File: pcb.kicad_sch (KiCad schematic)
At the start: 13 parts

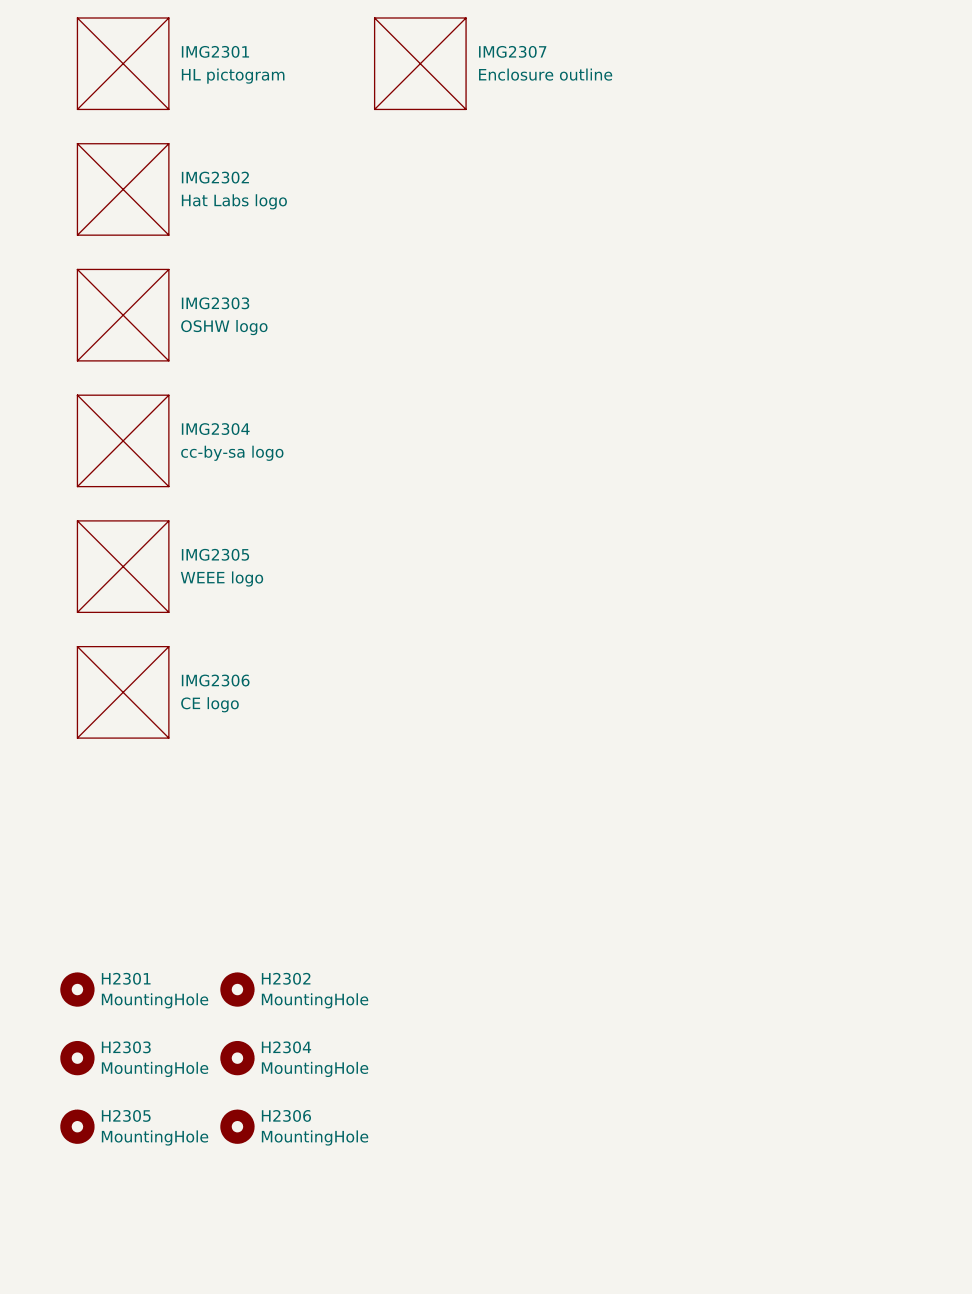
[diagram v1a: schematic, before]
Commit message: Reannotate components
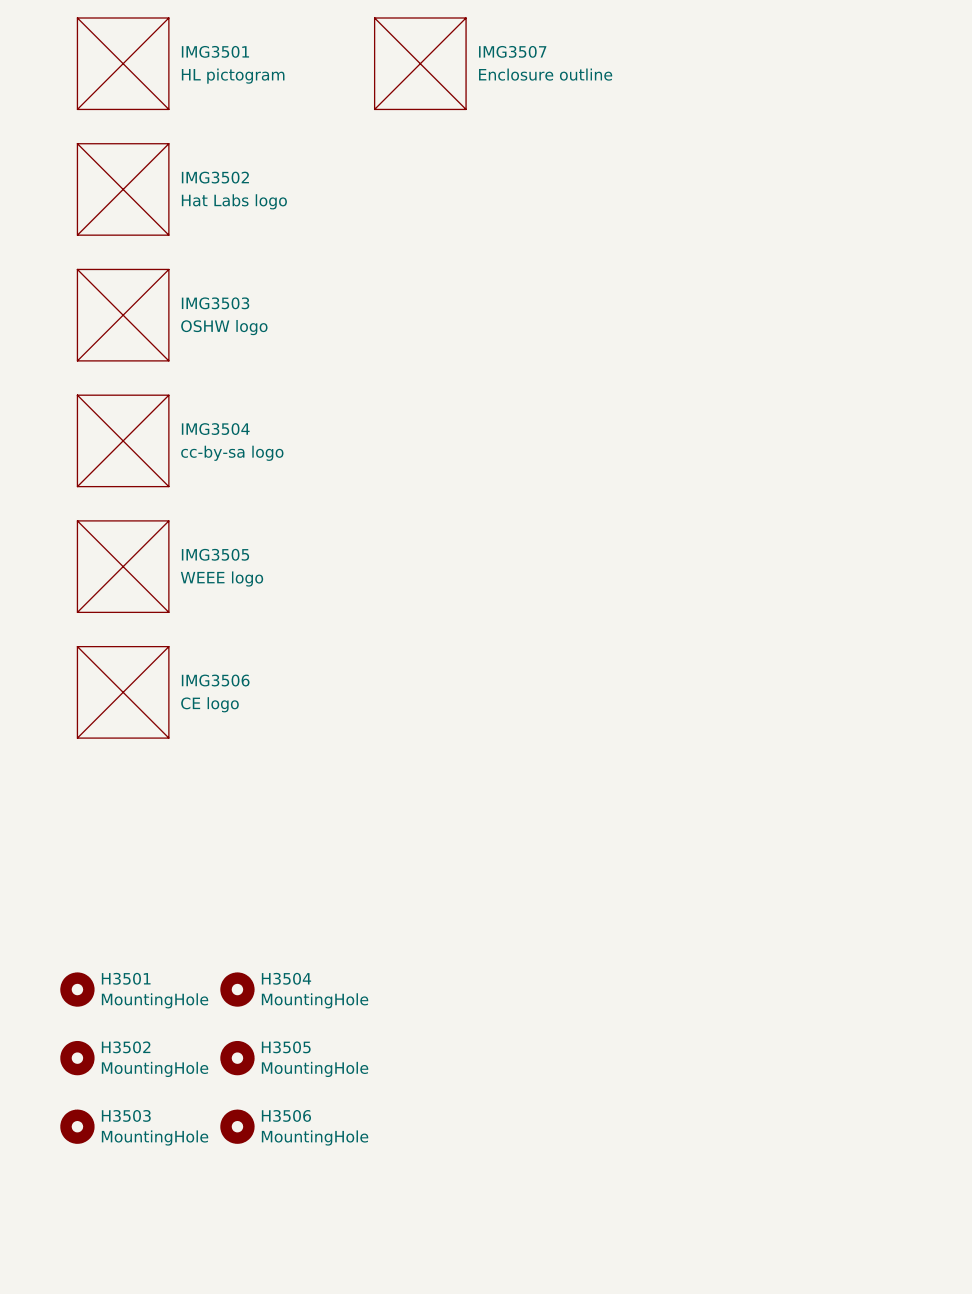
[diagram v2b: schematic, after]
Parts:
- renumbered H2301 to H3501, H2303 to H3502, H2305 to H3503, H2302 to H3504, H2304 to H3505, H2306 to H3506, IMG2301 to IMG3501, IMG2302 to IMG3502, IMG2303 to IMG3503, IMG2304 to IMG3504, IMG2305 to IMG3505, IMG2306 to IMG3506, IMG2307 to IMG3507
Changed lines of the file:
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@@
 		(dnp no)
 		(fields_autoplaced yes)
-		(property "Reference" "IMG2305"
+		(property "Reference" "IMG3505"
 			(at 52.07 92.7099 0)
 			(effects
@@
 			(project "HALPI2"
 				(path "/abc482bd-3f17-4d35-80db-1da3dcdb5c27/e4643111-53ad-48d1-8ad1-a500e184f609"
-					(reference "IMG2305")
+					(reference "IMG3505")
 					(unit 1)
 				)
@@
 		(on_board yes)
 		(dnp no)
-		(property "Reference" "H2306"
+		(property "Reference" "H3506"
 			(at 60.9601 155.0606 0)
 			(effects
@@
 			(project "HALPI2"
 				(path "/abc482bd-3f17-4d35-80db-1da3dcdb5c27/e4643111-53ad-48d1-8ad1-a500e184f609"
-					(reference "H2306")
+					(reference "H3506")
 					(unit 1)
 				)
@@
 		(dnp no)
 		(fields_autoplaced yes)
-		(property "Reference" "IMG2302"
+		(property "Reference" "IMG3502"
 			(at 52.07 50.7999 0)
 			(effects
@@
 			(project "HALPI2"
 				(path "/abc482bd-3f17-4d35-80db-1da3dcdb5c27/e4643111-53ad-48d1-8ad1-a500e184f609"
-					(reference "IMG2302")
+					(reference "IMG3502")
 					(unit 1)
 				)
@@
 		(dnp no)
 		(fields_autoplaced yes)
-		(property "Reference" "IMG2303"
+		(property "Reference" "IMG3503"
 			(at 52.07 64.7699 0)
 			(effects
@@
 			(project "HALPI2"
 				(path "/abc482bd-3f17-4d35-80db-1da3dcdb5c27/e4643111-53ad-48d1-8ad1-a500e184f609"
-					(reference "IMG2303")
+					(reference "IMG3503")
 					(unit 1)
 				)
@@
 		(on_board yes)
 		(dnp no)
-		(property "Reference" "H2302"
+		(property "Reference" "H3504"
 			(at 60.9601 139.8206 0)
 			(effects
@@
 			(project "HALPI2"
 				(path "/abc482bd-3f17-4d35-80db-1da3dcdb5c27/e4643111-53ad-48d1-8ad1-a500e184f609"
-					(reference "H2302")
+					(reference "H3504")
 					(unit 1)
 				)
@@
 		(on_board yes)
 		(dnp no)
-		(property "Reference" "H2304"
+		(property "Reference" "H3505"
 			(at 60.9601 147.4406 0)
 			(effects
@@
 			(project "HALPI2"
 				(path "/abc482bd-3f17-4d35-80db-1da3dcdb5c27/e4643111-53ad-48d1-8ad1-a500e184f609"
-					(reference "H2304")
+					(reference "H3505")
 					(unit 1)
 				)
@@
 		(on_board yes)
 		(dnp no)
-		(property "Reference" "H2303"
+		(property "Reference" "H3502"
 			(at 43.1801 147.4406 0)
 			(effects
@@
 			(project "HALPI2"
 				(path "/abc482bd-3f17-4d35-80db-1da3dcdb5c27/e4643111-53ad-48d1-8ad1-a500e184f609"
-					(reference "H2303")
+					(reference "H3502")
 					(unit 1)
 				)
@@
 		(dnp no)
 		(fields_autoplaced yes)
-		(property "Reference" "IMG2304"
+		(property "Reference" "IMG3504"
 			(at 52.07 78.7399 0)
 			(effects
@@
 			(project "HALPI2"
 				(path "/abc482bd-3f17-4d35-80db-1da3dcdb5c27/e4643111-53ad-48d1-8ad1-a500e184f609"
-					(reference "IMG2304")
+					(reference "IMG3504")
 					(unit 1)
 				)
@@
 		(dnp no)
 		(fields_autoplaced yes)
-		(property "Reference" "IMG2307"
+		(property "Reference" "IMG3507"
 			(at 85.09 36.8299 0)
 			(effects
@@
 			(project "HALPI2"
 				(path "/abc482bd-3f17-4d35-80db-1da3dcdb5c27/e4643111-53ad-48d1-8ad1-a500e184f609"
-					(reference "IMG2307")
+					(reference "IMG3507")
 					(unit 1)
 				)
@@
 		(on_board yes)
 		(dnp no)
-		(property "Reference" "H2301"
+		(property "Reference" "H3501"
 			(at 43.1801 139.8206 0)
 			(effects
@@
 			(project "HALPI2"
 				(path "/abc482bd-3f17-4d35-80db-1da3dcdb5c27/e4643111-53ad-48d1-8ad1-a500e184f609"
-					(reference "H2301")
+					(reference "H3501")
 					(unit 1)
 				)
@@
 		(dnp no)
 		(fields_autoplaced yes)
-		(property "Reference" "IMG2301"
+		(property "Reference" "IMG3501"
 			(at 52.07 36.8299 0)
 			(effects
@@
 			(project "HALPI2"
 				(path "/abc482bd-3f17-4d35-80db-1da3dcdb5c27/e4643111-53ad-48d1-8ad1-a500e184f609"
-					(reference "IMG2301")
+					(reference "IMG3501")
 					(unit 1)
 				)
@@
 		(on_board yes)
 		(dnp no)
-		(property "Reference" "H2305"
+		(property "Reference" "H3503"
 			(at 43.1801 155.0606 0)
 			(effects
@@
 			(project "HALPI2"
 				(path "/abc482bd-3f17-4d35-80db-1da3dcdb5c27/e4643111-53ad-48d1-8ad1-a500e184f609"
-					(reference "H2305")
+					(reference "H3503")
 					(unit 1)
 				)
@@
 		(dnp no)
 		(fields_autoplaced yes)
-		(property "Reference" "IMG2306"
+		(property "Reference" "IMG3506"
 			(at 52.07 106.6799 0)
 			(effects
@@
 			(project "HALPI2"
 				(path "/abc482bd-3f17-4d35-80db-1da3dcdb5c27/e4643111-53ad-48d1-8ad1-a500e184f609"
-					(reference "IMG2306")
-					(unit 1)
-				)
+					(reference "IMG3506")
+					(unit 1)
+				)

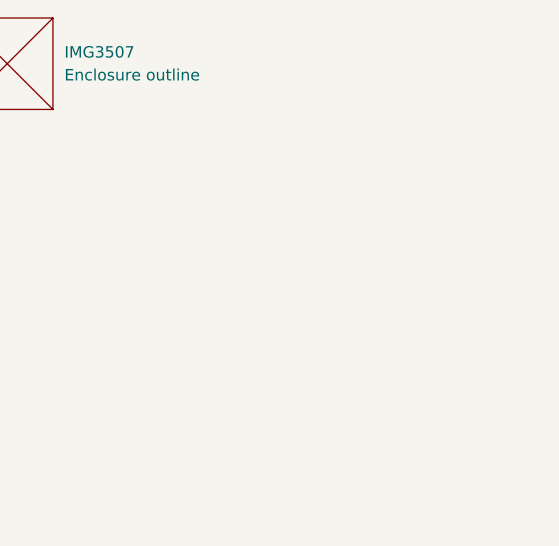
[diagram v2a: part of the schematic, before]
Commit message: Most DRC errors fixed
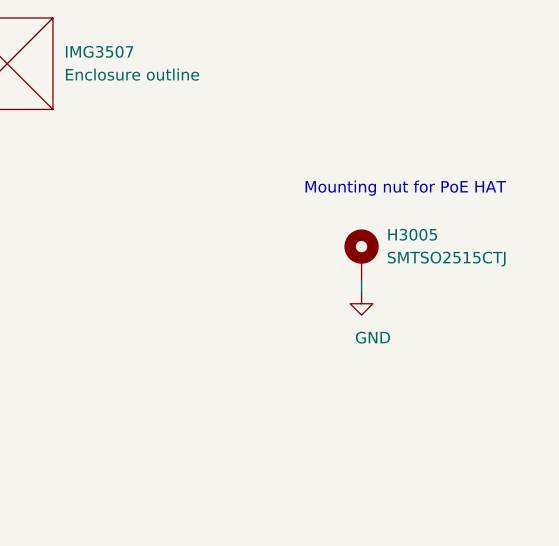
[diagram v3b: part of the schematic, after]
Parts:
- added H3005: SMTSO2515CTJ, Hatlabs:SMTSO2515CTJ, symbol Mechanical:MountingHole_Pad
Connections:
- new net GND: H3005.1
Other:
- note added: "Mounting nut for PoE HAT"
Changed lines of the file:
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@@
 		(comment 3 "HALPI2 is licensed under CERN-OHL-S v2.")
+	)
+	(text "Mounting nut for PoE HAT"
+		(exclude_from_sim no)
+		(at 122.936 52.07 0)
+		(effects
+			(font
+				(size 1.27 1.27)
+			)
+		)
+	)
+	(wire
+		(pts
+			(xy 118.11 63.5) (xy 118.11 62.23)
+		)
+		(stroke
+			(width 0)
+			(type default)
+		)
 	)
 	(symbol
@@
 	)
 	(symbol
+		(lib_id "power:GND")
+		(at 118.11 63.5 0)
+		(unit 1)
+		(exclude_from_sim no)
+		(in_bom yes)
+		(on_board yes)
+		(dnp no)
+		(property "Reference" "#PWR03009"
+			(at 118.11 69.85 0)
+			(effects
+				(font
+					(size 1.27 1.27)
+				)
+				(hide yes)
+			)
+		)
+		(property "Value" "GND"
+			(at 119.38 68.58 0)
+			(effects
+				(font
+					(size 1.27 1.27)
+				)
+			)
+		)
+		(property "Footprint" ""
+			(at 118.11 63.5 0)
+			(effects
+				(font
+					(size 1.27 1.27)
+				)
+				(hide yes)
+			)
+		)
+		(property "Datasheet" ""
+			(at 118.11 63.5 0)
+			(effects
+				(font
+					(size 1.27 1.27)
+				)
+				(hide yes)
+			)
+		)
+		(property "Description" "Power symbol creates a global label with name \"GND\" , ground"
+			(at 118.11 63.5 0)
+			(effects
+				(font
+					(size 1.27 1.27)
+				)
+				(hide yes)
+			)
+		)
+		(pin "1"
+		)
+		(instances
+			(project "HALPI2"
+				(path "/abc482bd-3f17-4d35-80db-1da3dcdb5c27/e4643111-53ad-48d1-8ad1-a500e184f609"
+					(reference "#PWR03009")
+					(unit 1)
+				)
+			)
+		)
+	)
+	(symbol
 		(lib_id "Mechanical:MountingHole")
 		(at 40.64 148.59 0)
@@
 					(unit 1)
 				)
+			)
+		)
+	)
+	(symbol
+		(lib_id "Mechanical:MountingHole_Pad")
+		(at 118.11 59.69 0)
+		(unit 1)
+		(exclude_from_sim no)
+		(in_bom yes)
+		(on_board yes)
+		(dnp no)
+		(fields_autoplaced yes)
+		(property "Reference" "H3005"
+			(at 120.904 57.1499 0)
+			(effects
+				(font
+					(size 1.27 1.27)
+				)
+				(justify left)
+			)
+		)
+		(property "Value" "SMTSO2515CTJ"
+			(at 120.904 59.6899 0)
+			(effects
+				(font
+					(size 1.27 1.27)
+				)
+				(justify left)
+			)
+		)
+		(property "Footprint" "Hatlabs:SMTSO2515CTJ"
+			(at 118.11 59.69 0)
+			(effects
+				(font
+					(size 1.27 1.27)
+				)
+				(hide yes)
+			)
+		)
+		(property "Datasheet" "~"
+			(at 118.11 59.69 0)
+			(effects
+				(font
+					(size 1.27 1.27)
+				)
+				(hide yes)
+			)
+		)
+		(property "Description" ""
+			(at 118.11 59.69 0)
+			(effects
+				(font
+					(size 1.27 1.27)
+				)
+				(hide yes)
+			)
+		)
+		(property "LCSC" "C2915629"
+			(at 118.11 59.69 0)
+			(effects
+				(font
+					(size 1.27 1.27)
+				)
+				(hide yes)
+			)
+		)
+		(property "Characteristics" ""
+			(at 118.11 59.69 0)
+			(effects
+				(font
+					(size 1.27 1.27)
+				)
+				(hide yes)
+			)
+		)
+		(pin "1"
+		)
+		(instances
+			(project "HALPI2"
+				(path "/abc482bd-3f17-4d35-80db-1da3dcdb5c27/e4643111-53ad-48d1-8ad1-a500e184f609"
+					(reference "H3005")
+					(unit 1)
+				)

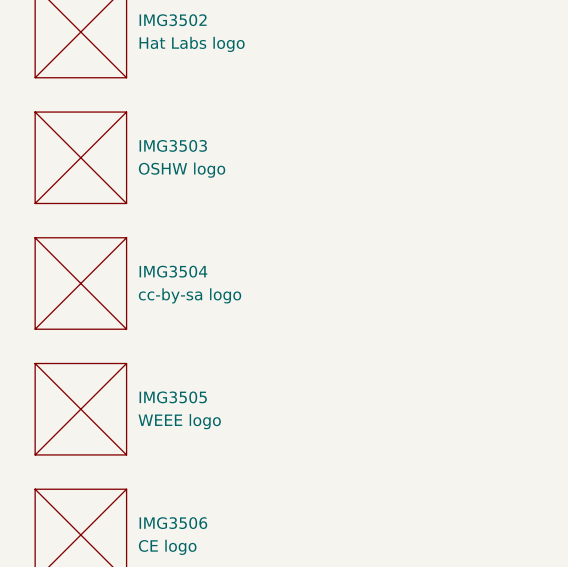
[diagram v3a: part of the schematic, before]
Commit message: Fix most DRC errors, partial silk screen
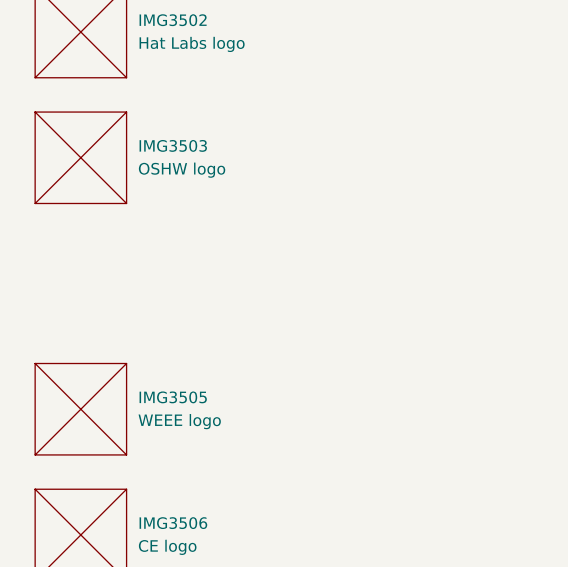
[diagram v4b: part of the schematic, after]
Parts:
- removed IMG3504: cc-by-sa logo, Hatlabs:cc-by-sa_silkscreen, symbol Hatlabs:SilkScreenImage
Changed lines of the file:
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@@
-	)
-	(symbol
-		(lib_id "Hatlabs:SilkScreenImage")
-		(at 45.72 77.47 0)
-		(unit 1)
-		(exclude_from_sim no)
-		(in_bom no)
-		(on_board yes)
-		(dnp no)
-		(fields_autoplaced yes)
-		(property "Reference" "IMG3504"
-			(at 52.07 78.7399 0)
-			(effects
-				(font
-					(size 1.27 1.27)
-				)
-				(justify left)
-			)
-		)
-		(property "Value" "cc-by-sa logo"
-			(at 52.07 81.2799 0)
-			(effects
-				(font
-					(size 1.27 1.27)
-				)
-				(justify left)
-			)
-		)
-		(property "Footprint" "Hatlabs:cc-by-sa_silkscreen"
-			(at 45.72 77.47 0)
-			(effects
-				(font
-					(size 1.27 1.27)
-				)
-				(hide yes)
-			)
-		)
-		(property "Datasheet" ""
-			(at 45.72 77.47 0)
-			(effects
-				(font
-					(size 1.27 1.27)
-				)
-				(hide yes)
-			)
-		)
-		(property "Description" ""
-			(at 45.72 77.47 0)
-			(effects
-				(font
-					(size 1.27 1.27)
-				)
-				(hide yes)
-			)
-		)
-		(property "Characteristics" ""
-			(at 45.72 77.47 0)
-			(effects
-				(font
-					(size 1.27 1.27)
-				)
-				(hide yes)
-			)
-		)
-		(instances
-			(project "HALPI2"
-				(path "/abc482bd-3f17-4d35-80db-1da3dcdb5c27/e4643111-53ad-48d1-8ad1-a500e184f609"
-					(reference "IMG3504")
-					(unit 1)
-				)
-			)
-		)
 	)
 	(symbol

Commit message: Silkscreen mostly done
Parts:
- H3501, H3502, H3503, H3504, H3505, H3506: footprint MountingHole:MountingHole_2.7mm_M2.5 -> MountingHole:MountingHole_2.2mm_M2_Pad_Via; symbol Mechanical:MountingHole -> Mechanical:MountingHole_Pad
- IMG3501: footprint Hatlabs:HL_pictogram_6.3mm -> Hatlabs:HL_picto_halftone_70mm
- IMG3502: footprint Hatlabs:Hat_Labs_25.4mm -> Hatlabs:Hat_Labs_13mm
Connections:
- net GND: now also H3501.1, H3502.1, H3503.1, H3504.1, H3505.1, H3506.1
